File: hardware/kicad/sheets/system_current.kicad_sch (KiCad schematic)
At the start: 5 parts, among them U20 INA237AIDGSR

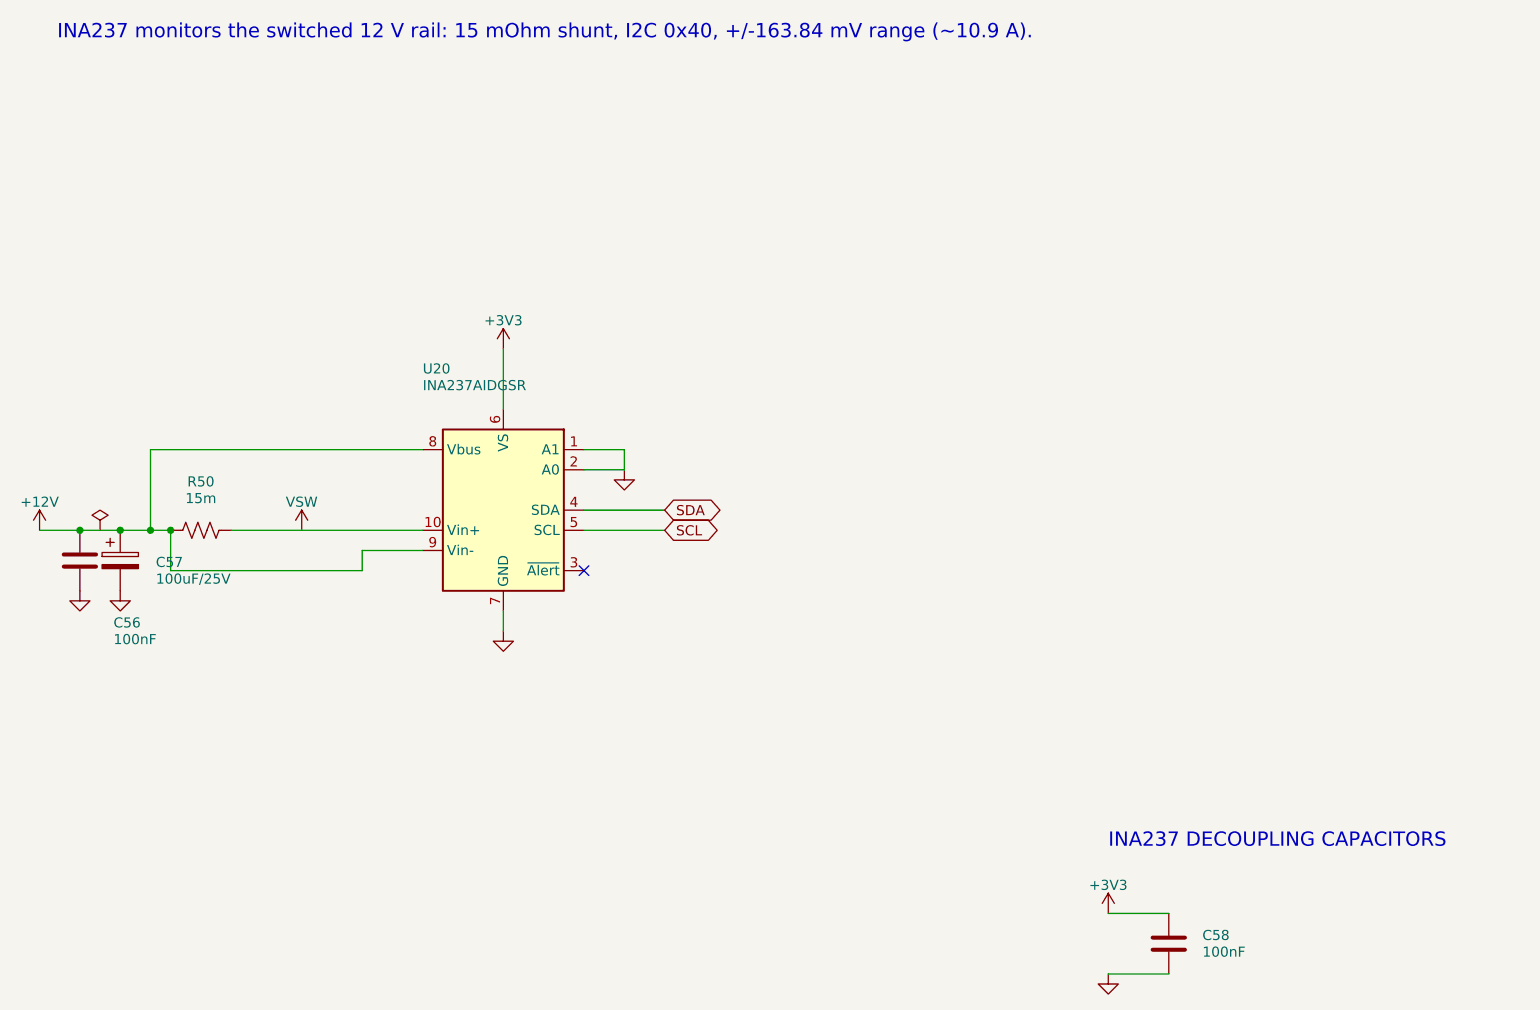
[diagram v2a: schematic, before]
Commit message: Fixing the UUID issues
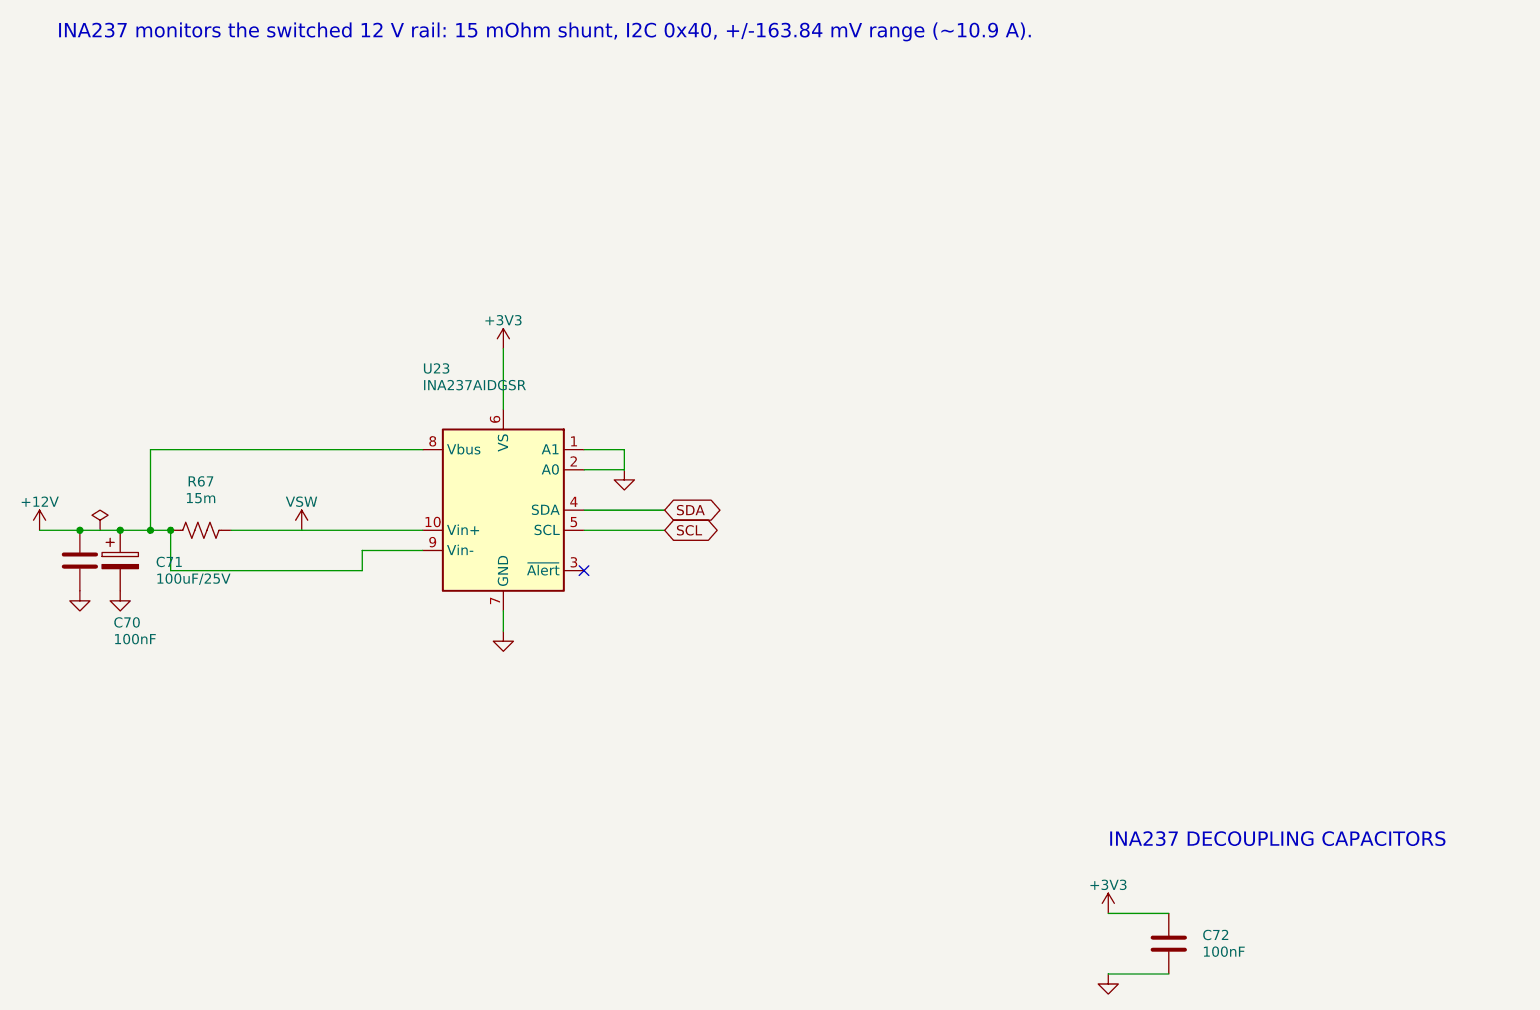
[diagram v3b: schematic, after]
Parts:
- removed C56: 100nF, Capacitor_SMD:C_0805_2012Metric, symbol Device:C
- removed C57: 100uF/25V, Capacitor_SMD:CP_Elec_8x10, symbol Device:C_Polarized
- removed C58: 100nF, Capacitor_SMD:C_0603_1608Metric, symbol Device:C
- removed R50: 15m, Resistor_SMD:R_2512_6332Metric, symbol Device:R_US
- removed U20: INA237AIDGSR, Package_SO:TSSOP-10_3x3mm_P0.5mm, symbol Sensor_Energy:INA237
- added C70: 100nF, Capacitor_SMD:C_0805_2012Metric, symbol Device:C
- added C71: 100uF/25V, Capacitor_SMD:CP_Elec_8x10, symbol Device:C_Polarized
- added C72: 100nF, Capacitor_SMD:C_0603_1608Metric, symbol Device:C
- added R67: 15m, Resistor_SMD:R_2512_6332Metric, symbol Device:R_US
- added U23: INA237AIDGSR, Package_SO:TSSOP-10_3x3mm_P0.5mm, symbol Sensor_Energy:INA237
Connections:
- net +12V: now also C70.1, C71.1, R67.1, U23.8 (Vbus), U23.9 (Vin-)
- net +3V3: now also C72.1, U23.6 (VS)
- net GND: now also C70.2, C71.2, C72.2, U23.1 (A1), U23.2 (A0), U23.7 (GND)
- net SCL: now also U23.5 (SCL)
- net SDA: now also U23.4 (SDA)
- net VSW: now also R67.2, U23.10 (Vin+)
